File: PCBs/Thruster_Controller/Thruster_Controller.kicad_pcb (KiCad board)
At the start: 4 copper layers, 36 x 37.5 mm, 110 parts, among them J1 PHASE_A, J2 PHASE_B, J3 PHASE_C, J4 Conn_01x01, J5 Pogo Conn, J6 Conn_01x01, J7 Conn_01x01, J8 Conn_01x01, Q1 SIZF906DT, Q2 SIZF906DT, Q3 SIZF906DT, U1 DRV8305, U2 RTQ2569-50GQW, U3 MCP2515, U4 TPS62172DSGR, U5 TMS320F28027F, U8 MCP2562, Y1 20MHz

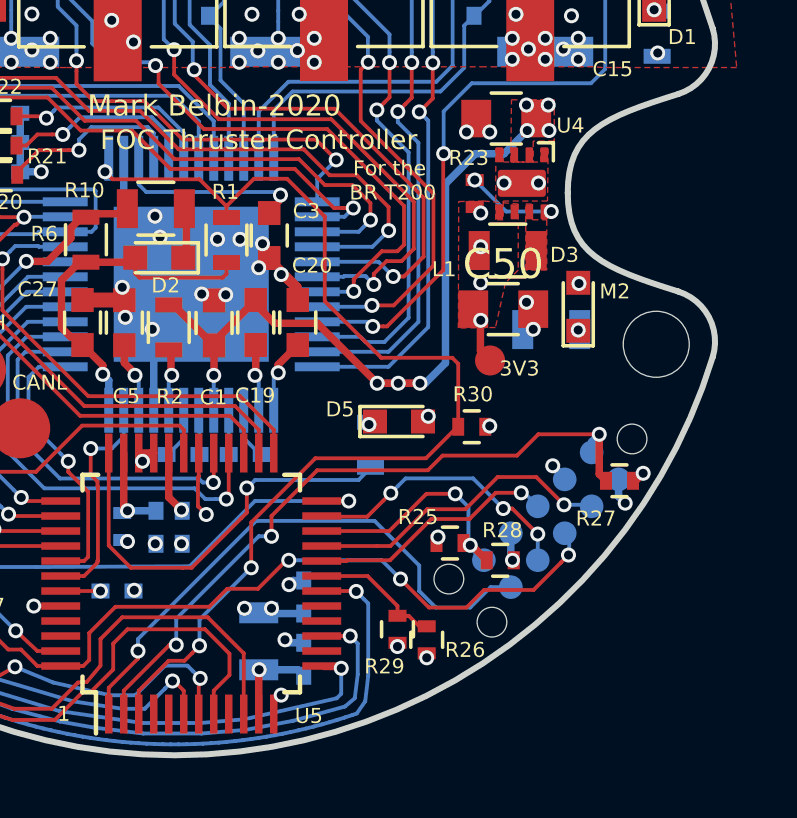
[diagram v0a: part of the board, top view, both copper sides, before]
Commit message: New Gerbers
- Fixed some small errors in silkscreen on the thruster controller
- Moved the programming header further from the edge, should help mechanically
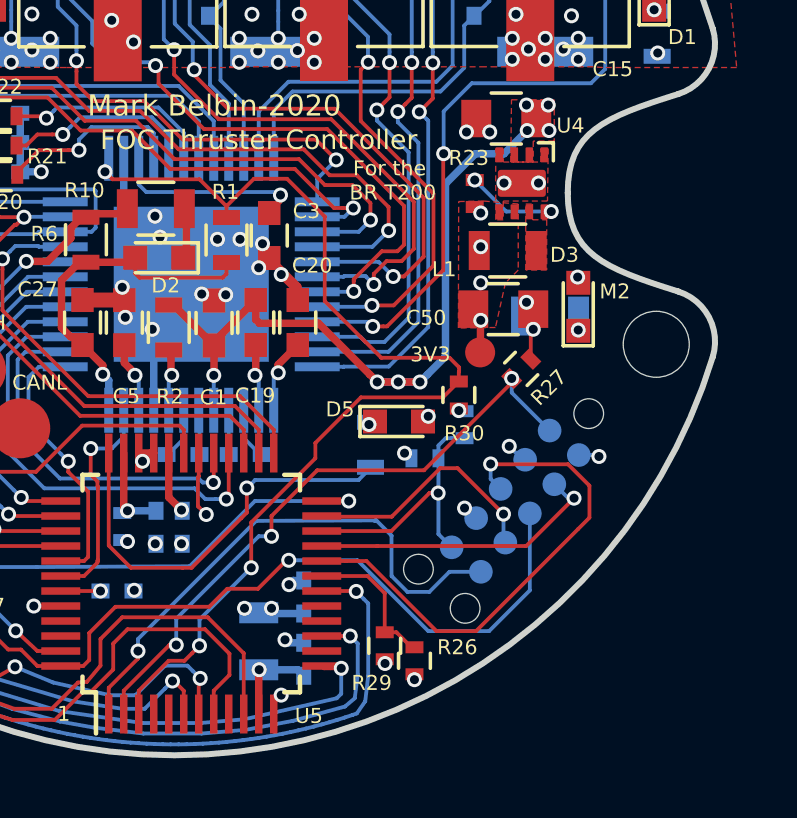
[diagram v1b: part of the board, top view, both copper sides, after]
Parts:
- R25, R28: moved to B.Cu
- moved R27 4.96 mm to (111.0, 105.3), turned to 45 degrees
- moved R28 4.23 mm to (107.8, 108.3), turned to 180 degrees
- moved R25 3.97 mm to (109.1, 107.2), turned to 270 degrees
- moved J5 1.35 mm to (110.8, 109.7), turned to 230 degrees
- moved R30 1.14 mm to (108.9, 106.2), turned to 90 degrees
- moved R26 0.81 mm to (107.4, 115.0)
- moved R29 0.70 mm to (106.5, 114.5)
- moved R19 0.45 mm to (112.0, 103.6)
- moved TP1 0.43 mm to (109.6, 104.8)
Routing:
- net /TDI: track 8.33 -> 17.1 mm
- net /TRST: track 23.4 -> 21.3 mm
- net /TCK: track 9.38 -> 8.35 mm, vias 3 -> 1
- net /GPIO29: track 18.9 -> 18.1 mm
- net +3V3: track 20.3 -> 19.6 mm, vias 17 -> 16
- net /GPIO28: track 43.8 -> 44.4 mm, vias 5 -> 3
- net /Powertrain/PWRGD: track 36.3 -> 35.7 mm
- net /TDO: track 8.59 -> 8.95 mm, vias 2 -> 1
